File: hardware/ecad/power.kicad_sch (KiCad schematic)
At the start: 22 parts, among them J1 USB_C_Receptacle, J2 Conn_01x02, U1 BQ24079RGTT, U2 TPS62162DSG, U3 TLV61047DDC

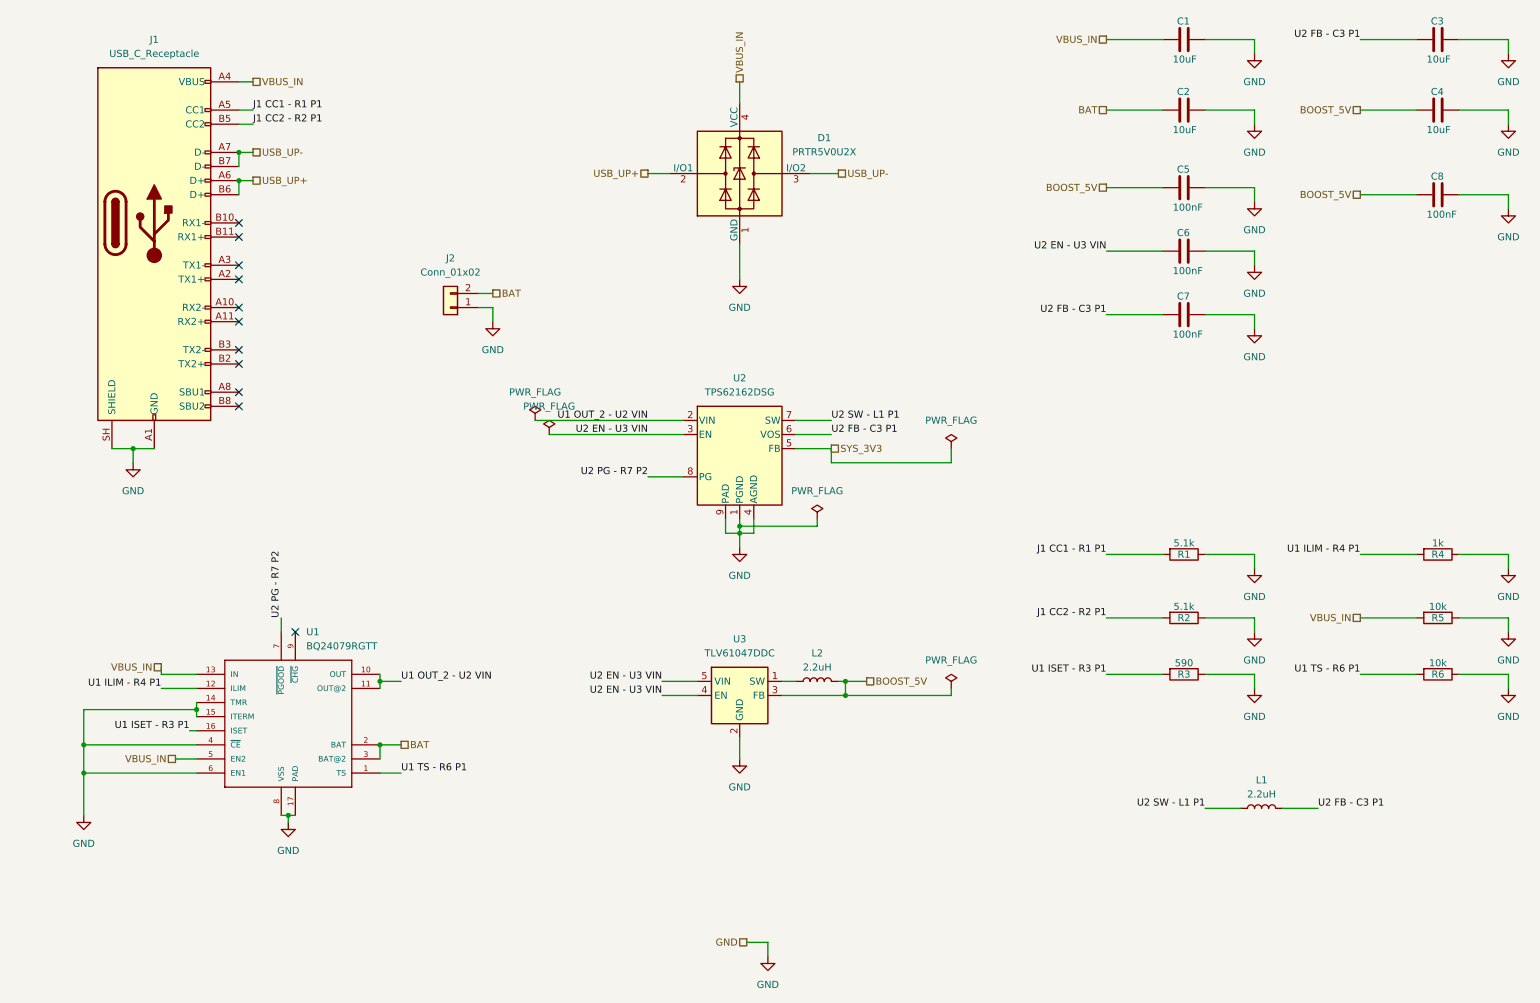
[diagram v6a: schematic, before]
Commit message: fix: resolve fatal power and USB switching errors
Replace TLV61047 boost converter with MT3608; add SS14 catch diode, 4.7µH inductor, and correct FB divider (180kΩ/51kΩ) for 5V output
Fix TPS62162DSG EN circular dependency; connect directly to U1_OUT
Fix TPS62162DSG FB pin; disconnect from SYS_3V3 and tie to GND
Fix TPS2116 power mux; remove series resistor on VIN1, add correct PR1 divider (100kΩ/27kΩ), tie MODE to VIN1 for priority mode
Fix TS3USB30E OE pin; tie directly to GND to keep switch always enabled
Add PGOOD pull-up resistor (10kΩ) to SYS_3V3 on BQ24079
Change ISET resistor from 590Ω to 680Ω for 1.3A charge current
Remove unnecessary R5 (10kΩ VBUS_IN to GND bleed resistor)
Add USB_STATUS net from TPS2116 ST pin to ESP32 IO38
Add PWR_FLAG to BOOST_5V and U1_OUT nets
Fix U1_PGOOD net label placement; separate from SYS_3V3 pull-up node
Add documentation boxes and truth tables to power and USB switching pages
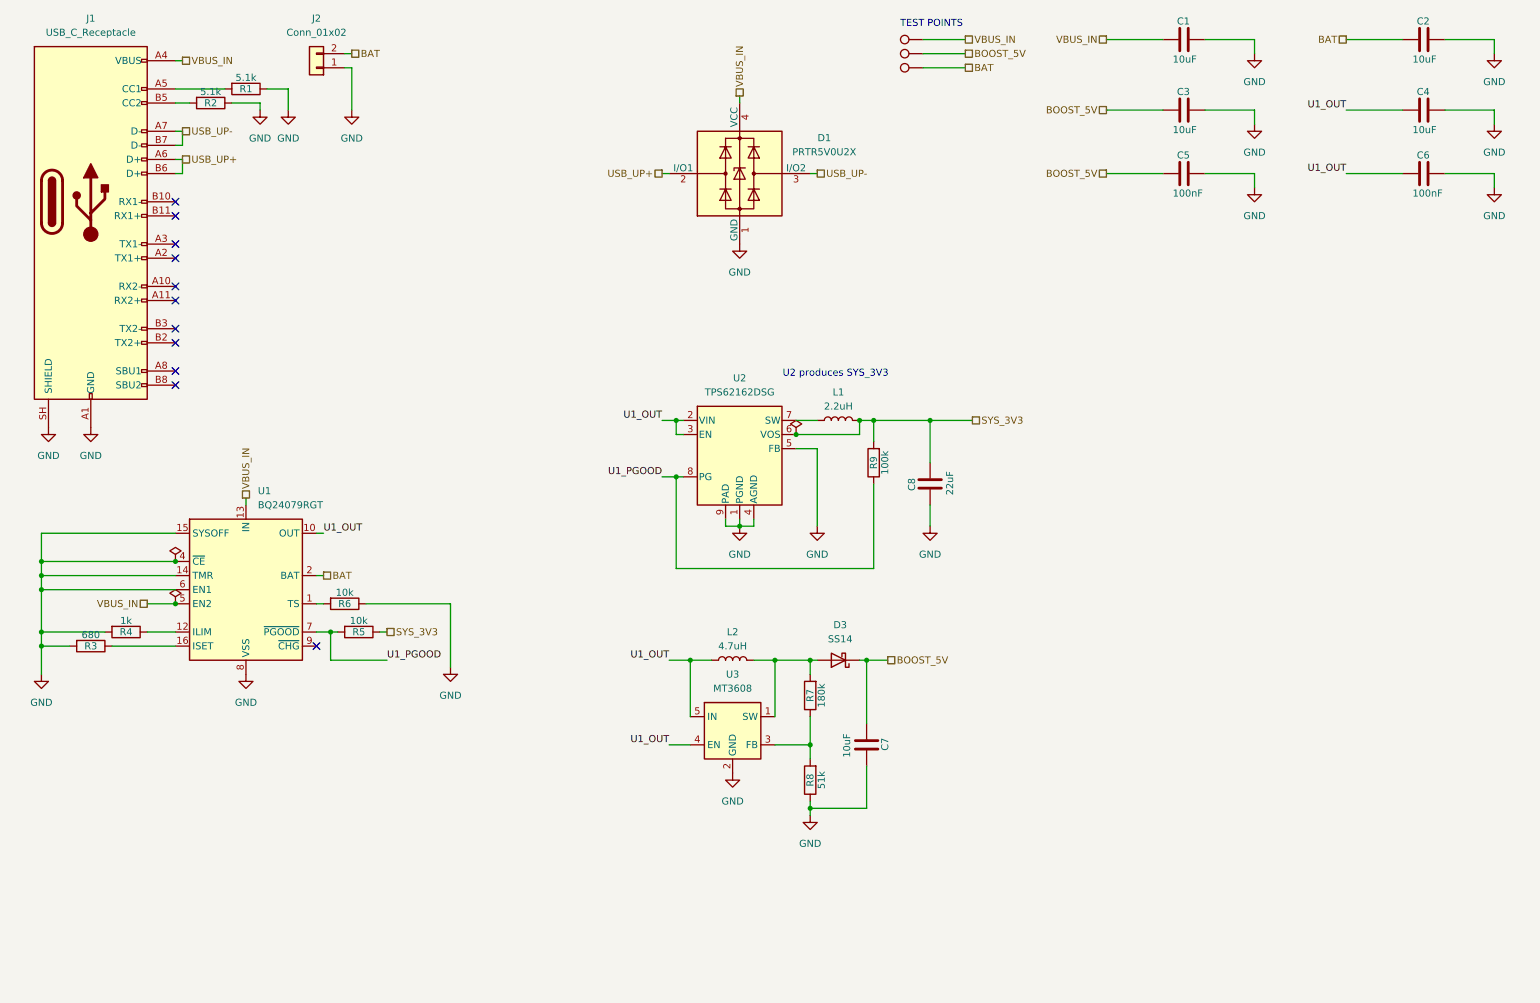
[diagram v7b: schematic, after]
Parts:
- removed C3: 10uF, Capacitor_SMD:C_0603_1608Metric, symbol Device:C
- removed U1: BQ24079RGTT, Package_DFN_QFN:VQFN-16-1EP_3x3mm_P0.5mm_EP1.68x1.68mm_ThermalVias, symbol BQ24074RGTT:BQ24074RGTT
- removed U3: TLV61047DDC, Package_TO_SOT_SMD:SOT-23-5, symbol Regulator_Switching:TLV61047DDC
- added C4: 10uF, Capacitor_SMD:C_0402_1005Metric, symbol Device:C
- added D3: SS14, Diode_SMD:D_SMA, symbol Diode:SS14
- added R7: 180k, Capacitor_SMD:C_0402_1005Metric, symbol Device:R
- added R8: 51k, Capacitor_SMD:C_0402_1005Metric, symbol Device:R
- added R9: 100k, Capacitor_SMD:C_0402_1005Metric, symbol Device:R
- added TP7, TP8, TP9: TestPoint, TestPoint:TestPoint_THTPad_D1.0mm_Drill0.5mm, symbol Connector:TestPoint
- added U1: BQ24079RGT, Package_DFN_QFN:VQFN-16-1EP_3x3mm_P0.5mm_EP1.6x1.6mm, symbol Battery_Management:BQ24079RGT
- added U3: MT3608, Package_TO_SOT_SMD:SOT-23-6, symbol Regulator_Switching:MT3608
- C7: value 100nF -> 10uF
- C8: value 100nF -> 22uF
- L2: value 2.2uH -> 4.7uH
- R3: value 590 -> 680
- renumbered C4 to C3
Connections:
- net U1 ILIM - R4 P1 is gone; now on net GND: R4.2
- net U1 ISET - R3 P1 is gone; now on net GND: R3.2
- net U1 OUT_2 - U2 VIN is gone; now on net U1_OUT: U2.2 (VIN)
- net U2 EN - U3 VIN is gone; now on net U1_OUT: C6.2, U2.3 (EN)
- net BAT: now also TP9.1, U1.2 (BAT), U1.3 (BAT)
- net BOOST_5V: now also C7.2, D3.1 (K), TP8.1; no longer C8.2, L2.2
- net GND: now also C8.2, U2.5 (FB), C4.1, R8.1, U1.14 (TMR), U1.15 (SYSOFF), U1.17 (VSS), U1.4 (~{CE}), U1.6 (EN1), U1.8 (VSS), U3.2 (GND); no longer C8.1, R3.1, R4.1, R5.1
- net SYS_3V3: now also C8.1, L1.2, R5.1, U2.6 (VOS), R9.2; no longer U2.5 (FB)
- net VBUS_IN: now also TP7.1, U1.13 (IN), U1.5 (EN2); no longer R5.2
- net U1_OUT: now reaches L2.1
- net U1_OUT: now also C4.2, U1.10 (OUT), U1.11 (OUT), U3.4 (EN), U3.5 (IN)
- net J1 CC1 - R1 P1: no longer names the net of J1.A5 (CC1), R1.2
- net J1 CC2 - R2 P1: no longer names the net of J1.B5 (CC2), R2.2
- net U1 TS - R6 P1: no longer names the net of R6.2
- net U1 TS - R6 P1: now also U1.1 (TS)
- removed net U2 FB - C3 P1: C7.2, L1.2, U2.6 (VOS)
- net U2 PG - R7 P2 renamed U1_PGOOD
- net U1_PGOOD: now also R5.2, R9.1, U1.7 (~{PGOOD})
- net U2 SW - L1 P1: no longer names the net of L1.1, U2.7 (SW)
- new net: D3.2 (A), L2.2, R7.2, U3.1 (SW)
- new net: R7.1, R8.2, U3.3 (FB)
- new net: R3.1, U1.16 (ISET)
- new net: R4.1, U1.12 (ILIM)
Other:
- note added: "TEST POINTS"
- note added: "U2 produces SYS_3V3"
- moved on the sheet: C2, C3, C5, J1, J2

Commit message: Fixed minor errors and smaller issues withing schematics, moved v1 pcb and specific projet artifacts to archive. Produced PDF of full schematic
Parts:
- removed J1: USB_C_Receptacle, Connector_USB:USB_C_Receptacle_Amphenol_12401610E4-2A_CircularHoles, symbol Connector:USB_C_Receptacle
- removed U1: BQ24079RGT, Package_DFN_QFN:VQFN-16-1EP_3x3mm_P0.5mm_EP1.6x1.6mm, symbol Battery_Management:BQ24079RGT
- added J1: USB_C_Receptacle_USB2.0_14P, Connector_USB:USB_C_Receptacle_G-Switch_GT-USB-7010ASV, symbol Connector:USB_C_Receptacle_USB2.0_14P
- added U1: BQ24075RGT, Package_DFN_QFN:VQFN-16-1EP_3x3mm_P0.5mm_EP1.6x1.6mm, symbol Battery_Management:BQ24075RGT
- C4, C5, C6, C7, C8: footprint Capacitor_SMD:C_0402_1005Metric -> Capacitor_SMD:C_0603_1608Metric
- R1, R2, R3, R4, R5, R6, R7, R8, R9: footprint Capacitor_SMD:C_0402_1005Metric -> Resistor_SMD:R_0603_1608Metric
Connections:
- net BAT: now also U1.2 (BAT), U1.3 (BAT)
- net GND: now also J1.A1 (GND), J1.A12 (GND), J1.B1 (GND), J1.B12 (GND), J1.SH (SHIELD), U1.14 (TMR), U1.15 (SYSOFF), U1.17 (VSS), U1.4 (~{CE}), U1.6 (EN1), U1.8 (VSS)
- net U1_OUT: now also U1.10 (OUT), U1.11 (OUT)
- net U1_PGOOD: now also U1.7 (~{PGOOD})
- net USB_UP+: now also J1.A6 (D+), J1.B6 (D+)
- net USB_UP-: now also J1.A7 (D-), J1.B7 (D-)
- net VBUS_IN: now also J1.A4 (VBUS), J1.A9 (VBUS), J1.B4 (VBUS), J1.B9 (VBUS), U1.13 (IN), U1.5 (EN2)
- net at R3.1: now also U1.16 (ISET)
- net at R1.2: now also J1.A5 (CC1)
- net at R6.2: now also U1.1 (TS)
- net at R4.1: now also U1.12 (ILIM)
- net at R2.2: now also J1.B5 (CC2)
- no-connect marks 11 -> 1
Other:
- moved on the sheet: J2, R1, R2
